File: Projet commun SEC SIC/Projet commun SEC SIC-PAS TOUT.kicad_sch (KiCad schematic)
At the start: 4 parts, among them J1 Conn_01x08_Female, J2 Conn_01x06_Female, J3 Conn_01x09_Female, U1 ATmega328-P

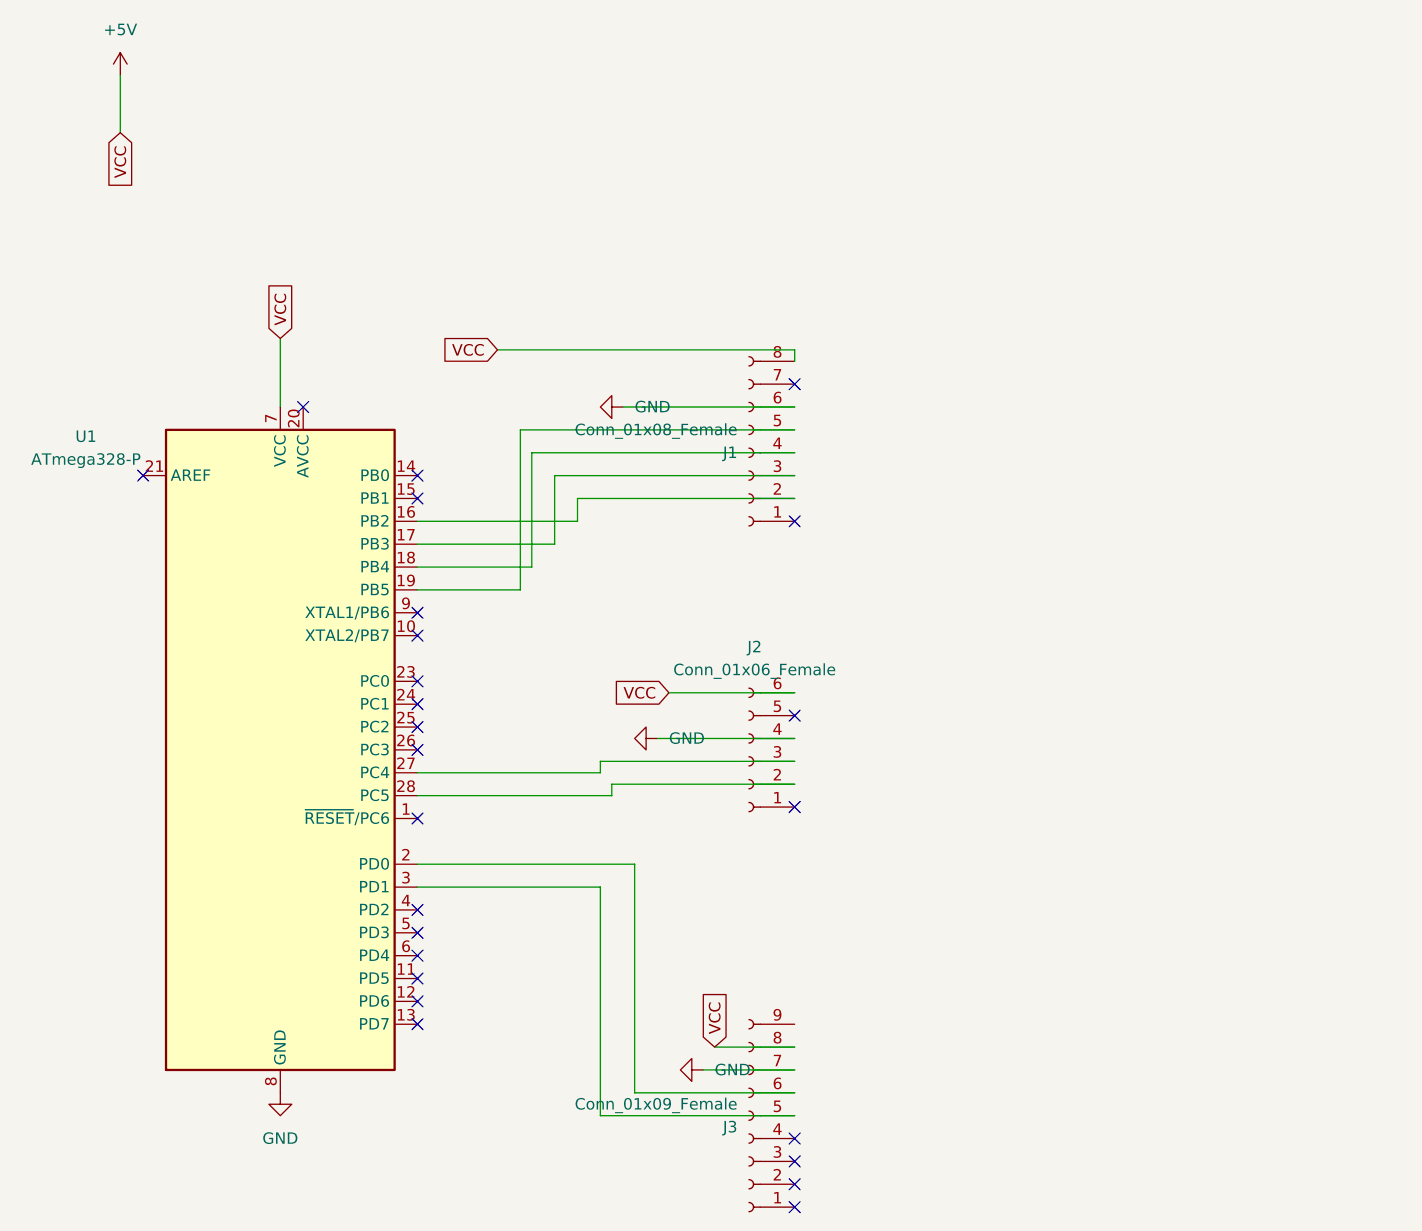
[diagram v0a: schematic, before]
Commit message: pcb avec bon pin & quartz & régulateur de tension
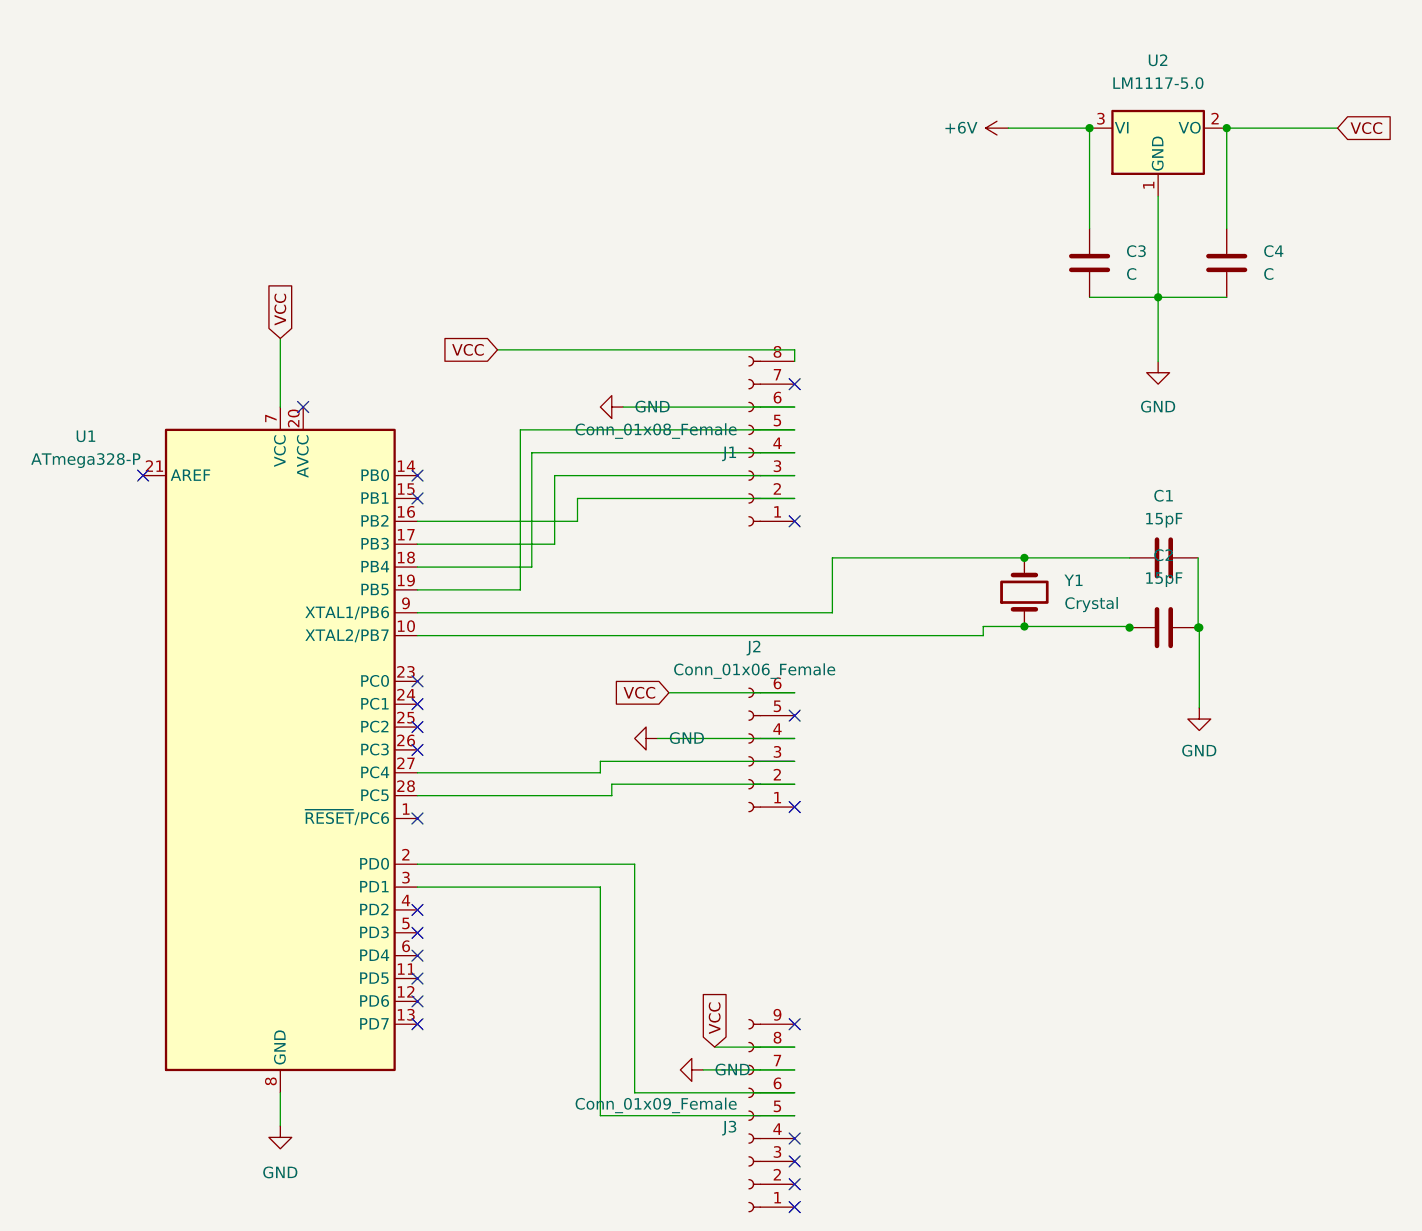
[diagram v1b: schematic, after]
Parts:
- added C1, C2: 15pF, Capacitor_SMD:C_1206_3216Metric, symbol Device:C
- added C3, C4: C, Capacitor_SMD:C_1206_3216Metric, symbol Device:C
- added U2: LM1117-5.0, eec:National_Semiconductor-LM1117IMP-5.0-Level_A, symbol Regulator_Linear:LM1117-5.0
- added Y1: Crystal, Crystal:Resonator-2Pin_W10.0mm_H5.0mm, symbol Device:Crystal
- J1: footprint Connector_PinHeader_1.00mm:PinHeader_1x08_P1.00mm_Vertical -> Connector_PinSocket_2.54mm:PinSocket_1x08_P2.54mm_Vertical
- J2: footprint Connector_PinHeader_1.00mm:PinHeader_1x06_P1.00mm_Vertical -> Connector_PinSocket_2.54mm:PinSocket_1x06_P2.54mm_Vertical
- J3: footprint Connector_PinHeader_1.00mm:PinHeader_1x09_P1.00mm_Vertical -> Connector_PinSocket_2.54mm:PinSocket_1x09_P2.54mm_Vertical
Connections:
- net GND: now also C1.2, C2.2, C3.2, C4.2, U2.1 (GND)
- net at U1.10 (XTAL2/PB7): now also C2.1, Y1.1
- net at U1.9 (XTAL1/PB6): now also C1.1, Y1.2
- net +5V renamed VCC
- net VCC: now also C4.1, U2.2 (VO)
- new net +6V: C3.1, U2.3 (VI)
- no-connect marks 25 -> 24

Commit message: PCB fini
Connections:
- net GND: now also C1.1, C2.1, J1.8 (Pin_8); no longer C1.2, C2.2, J1.6 (Pin_6)
- net VCC: now also J1.3 (Pin_3); no longer J1.8 (Pin_8)
- net at U1.10 (XTAL2/PB7), Y1.1: now also C2.2; no longer C2.1
- net at U1.16 (PB2): no longer J1.2 (Pin_2)
- net at U1.17 (PB3): now also J1.5 (Pin_5); no longer J1.3 (Pin_3)
- net at U1.18 (PB4): now also J1.7 (Pin_7); no longer J1.4 (Pin_4)
- net at U1.19 (PB5): now also J1.6 (Pin_6); no longer J1.5 (Pin_5)
- net at U1.6 (PD4): now also J1.4 (Pin_4)
- net at U1.9 (XTAL1/PB6), Y1.2: now also C1.2; no longer C1.1
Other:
- moved on the sheet: C1, C2
